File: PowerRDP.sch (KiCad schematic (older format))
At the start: 50 parts, among them J1 Conn_01x02_Male, J10 SOCKET, J11 FAA LED, J12 Switch, J13 Conn_Coaxial, J14 Conn_Coaxial, J15 Conn_Coaxial, J2 Conn_01x02_Male, J3 Conn_01x02_Male, J4 Conn_01x02_Male, J5 Conn_01x02_Male, J6 Conn_01x02_Male, J7 3.3V, J8 5V, J9 12V, Q1 NTR4003NT1G, U1 Recom_RS3, U2 LM2575-3.3BU, U3 LM2575-5.0BU, U4 LM2575-12BU, U5 TS555, U6 MCP602, U7 MCP602

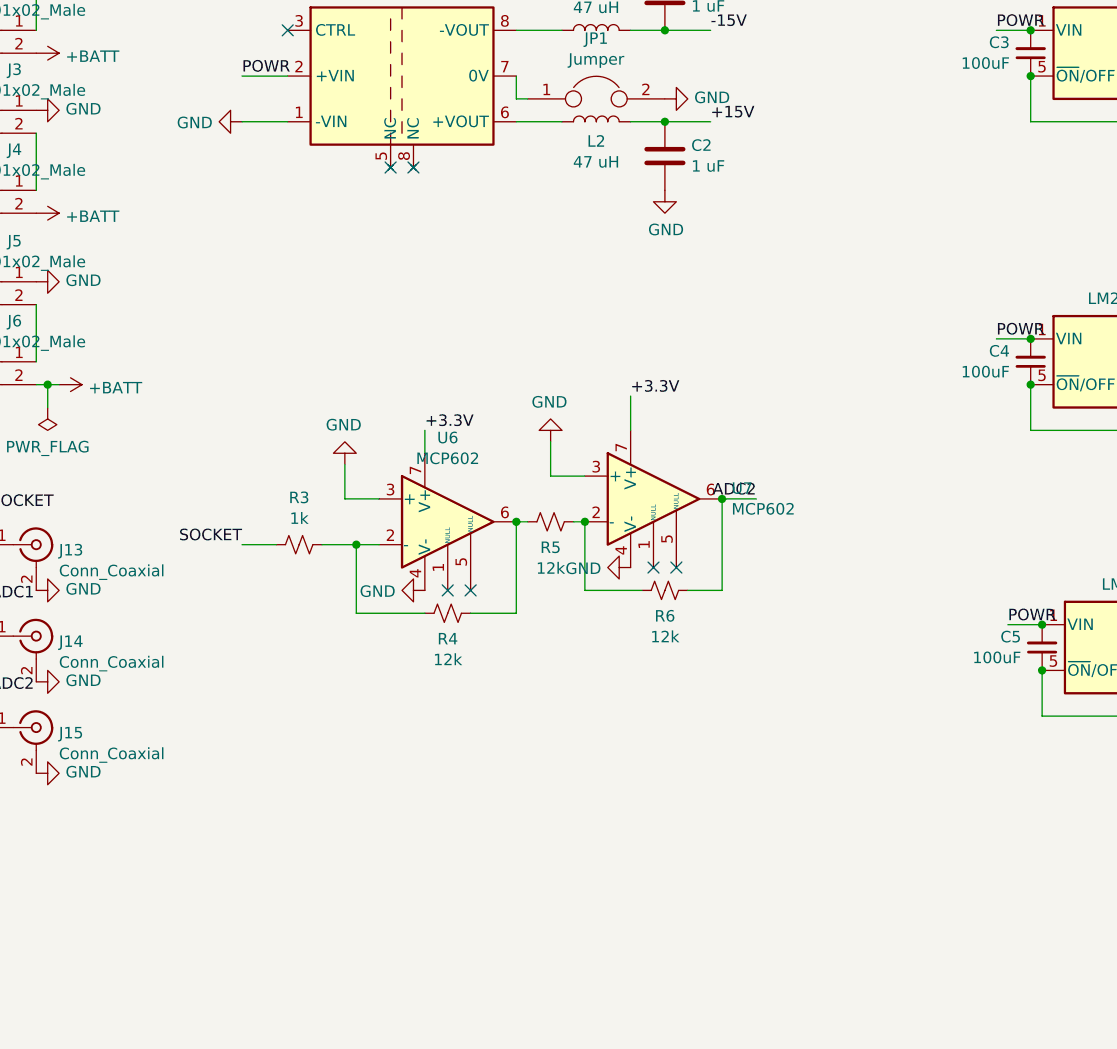
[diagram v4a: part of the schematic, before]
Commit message: Fix opamps by adding -V supply
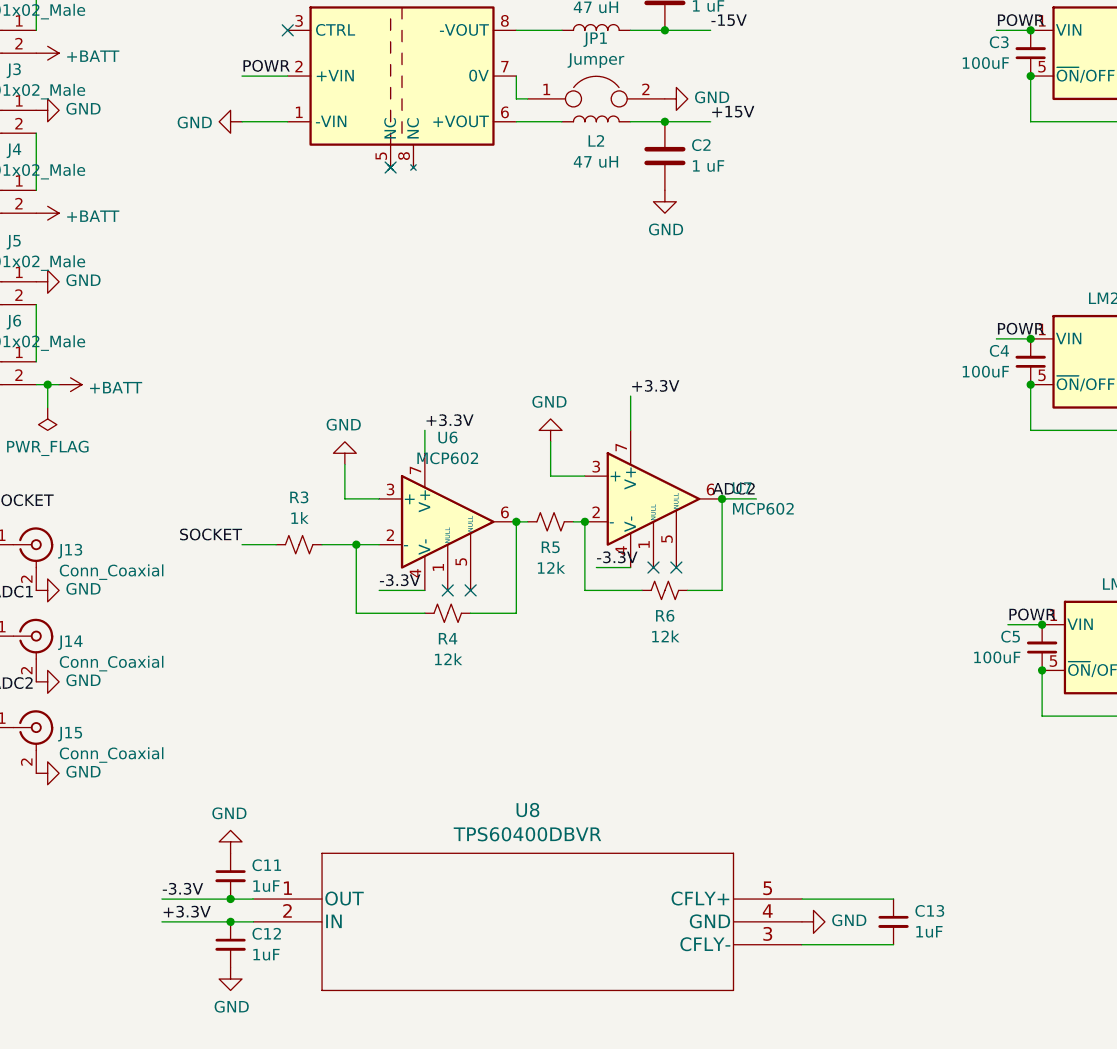
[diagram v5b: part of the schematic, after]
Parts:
- added C11, C12, C13: 1uF, Capacitor_SMD:C_0805_2012Metric_Pad1.15x1.40mm_HandSolder, symbol Device:C_Small
- added U8: TPS60400DBVR, footprints:TPS60400DBVR, symbol 2019-02-12_19-34-35:TPS60400DBVR
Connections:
- net +3.3V: now also C12.1, U8.2 (IN)
- net GND: now also C11.1, C12.2, U8.4 (GND); no longer U6.4 (V-), U7.4 (V-)
- new net: C13.2, U8.3 (CFLY-)
- new net: C13.1, U8.5 (CFLY+)
- new net -3.3V: C11.2, U6.4 (V-), U7.4 (V-), U8.1 (OUT)
- no-connect marks 7 -> 6
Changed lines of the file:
@@
 Wire Wire Line
 	9500 3000 9550 3000
-NoConn ~ 2850 1750
 NoConn ~ 2750 1750
 $Comp
@@
 Text Label 3800 2750 0    50   ~ 0
 +3.3V
-$Comp
-L power:GND #PWR0106
-U 1 1 5C712204
-P 2900 3600
-F 0 "#PWR0106" H 2900 3350 50  0001 C CNN
-F 1 "GND" V 2905 3472 50  0000 R CNN
-F 2 "" H 2900 3600 50  0001 C CNN
-F 3 "" H 2900 3600 50  0001 C CNN
-	1    2900 3600
-	0    1    1    0
-$EndComp
-$Comp
-L power:GND #PWR0107
-U 1 1 5C7122EE
-P 3800 3500
-F 0 "#PWR0107" H 3800 3250 50  0001 C CNN
-F 1 "GND" V 3805 3372 50  0000 R CNN
-F 2 "" H 3800 3500 50  0001 C CNN
-F 3 "" H 3800 3500 50  0001 C CNN
-	1    3800 3500
-	0    1    1    0
-$EndComp
 NoConn ~ 3000 3600
 NoConn ~ 3100 3600
@@
 Wire Wire Line
 	2900 2900 2900 3000
+$Comp
+L 2019-02-12_19-34-35:TPS60400DBVR U8
+U 1 1 5C731337
+P 2150 4950
+F 0 "U8" H 3350 5337 60  0000 C CNN
+F 1 "TPS60400DBVR" H 3350 5231 60  0000 C CNN
+F 2 "footprints:TPS60400DBVR" H 3350 5190 60  0001 C CNN
+F 3 "" H 2150 4950 60  0000 C CNN
+	1    2150 4950
+	1    0    0    -1
+$EndComp
+$Comp
+L Device:C_Small C12
+U 1 1 5C7316A0
+P 2050 5150
+F 0 "C12" H 2142 5196 50  0000 L CNN
+F 1 "1uF" H 2142 5105 50  0000 L CNN
+F 2 "Capacitor_SMD:C_0805_2012Metric_Pad1.15x1.40mm_HandSolder" H 2050 5150 50  0001 C CNN
+F 3 "~" H 2050 5150 50  0001 C CNN
+	1    2050 5150
+	1    0    0    -1
+$EndComp
+$Comp
+L Device:C_Small C11
+U 1 1 5C731818
+P 2050 4850
+F 0 "C11" H 2142 4896 50  0000 L CNN
+F 1 "1uF" H 2142 4805 50  0000 L CNN
+F 2 "Capacitor_SMD:C_0805_2012Metric_Pad1.15x1.40mm_HandSolder" H 2050 4850 50  0001 C CNN
+F 3 "~" H 2050 4850 50  0001 C CNN
+	1    2050 4850
+	1    0    0    -1
+$EndComp
+$Comp
+L Device:C_Small C13
+U 1 1 5C7318DF
+P 4950 5050
+F 0 "C13" H 5042 5096 50  0000 L CNN
+F 1 "1uF" H 5042 5005 50  0000 L CNN
+F 2 "Capacitor_SMD:C_0805_2012Metric_Pad1.15x1.40mm_HandSolder" H 4950 5050 50  0001 C CNN
+F 3 "~" H 4950 5050 50  0001 C CNN
+	1    4950 5050
+	1    0    0    -1
+$EndComp
+Wire Wire Line
+	1750 5050 2050 5050
+Connection ~ 2050 5050
+Wire Wire Line
+	2050 5050 2150 5050
+Wire Wire Line
+	1750 4950 2050 4950
+Connection ~ 2050 4950
+Wire Wire Line
+	2050 4950 2150 4950
+Wire Wire Line
+	4550 4950 4950 4950
+Wire Wire Line
+	4550 5150 4950 5150
+$Comp
+L power:GND #PWR0106
+U 1 1 5C744C44
+P 2050 5250
+F 0 "#PWR0106" H 2050 5000 50  0001 C CNN
+F 1 "GND" H 2055 5077 50  0000 C CNN
+F 2 "" H 2050 5250 50  0001 C CNN
+F 3 "" H 2050 5250 50  0001 C CNN
+	1    2050 5250
+	1    0    0    -1
+$EndComp
+$Comp
+L power:GND #PWR0107
+U 1 1 5C744D08
+P 2050 4750
+F 0 "#PWR0107" H 2050 4500 50  0001 C CNN
+F 1 "GND" H 2055 4577 50  0000 C CNN
+F 2 "" H 2050 4750 50  0001 C CNN
+F 3 "" H 2050 4750 50  0001 C CNN
+	1    2050 4750
+	-1   0    0    1
+$EndComp
+$Comp
+L power:GND #PWR0108
+U 1 1 5C744E38
+P 4550 5050
+F 0 "#PWR0108" H 4550 4800 50  0001 C CNN
+F 1 "GND" V 4555 4922 50  0000 R CNN
+F 2 "" H 4550 5050 50  0001 C CNN
+F 3 "" H 4550 5050 50  0001 C CNN
+	1    4550 5050
+	0    -1   -1   0
+$EndComp
+Text Label 1750 5050 0    50   ~ 0
++3.3V
+Text Label 1750 4950 0    50   ~ 0
+-3.3V
+Wire Wire Line
+	3650 3500 3800 3500
+Wire Wire Line
+	2700 3600 2900 3600
+Text Label 2700 3600 0    50   ~ 0
+-3.3V
+Text Label 3650 3500 0    50   ~ 0
+-3.3V
 $EndSCHEMATC

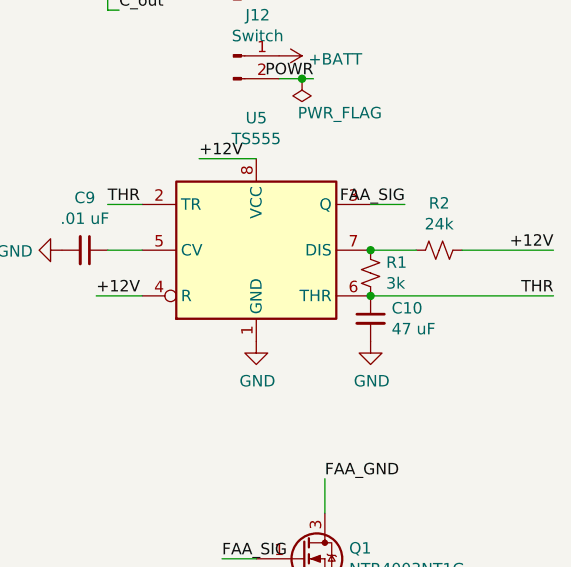
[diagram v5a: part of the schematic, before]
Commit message: Update 555 timer resistor value to new 50% duty cycle
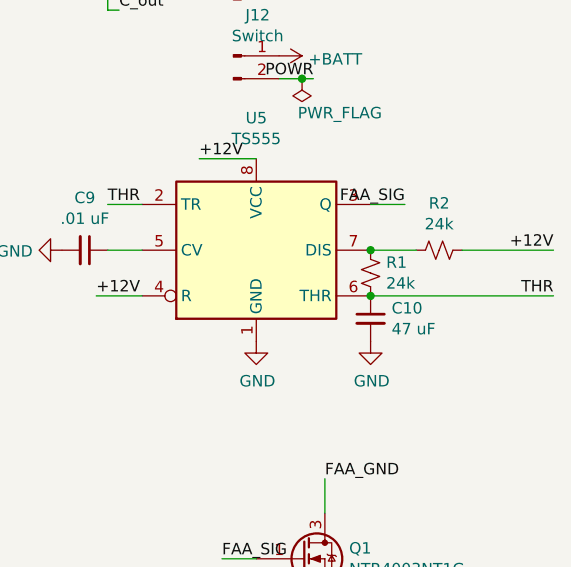
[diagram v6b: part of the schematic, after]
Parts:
- R1: value 3k -> 24k
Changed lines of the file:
@@
 EESchema Schematic File Version 4
 LIBS:PowerRDP-cache
-EELAYER 26 0
+EELAYER 29 0
 EELAYER END
 $Descr A4 11693 8268
@@
 P 9800 3850
 F 0 "R1" H 9868 3896 50  0000 L CNN
-F 1 "3k" H 9868 3805 50  0000 L CNN
+F 1 "24k" H 9868 3805 50  0000 L CNN
 F 2 "Resistor_SMD:R_0805_2012Metric_Pad1.15x1.40mm_HandSolder" H 9800 3850 50  0001 C CNN
 F 3 "~" H 9800 3850 50  0001 C CNN
